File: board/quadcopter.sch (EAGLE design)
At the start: 41 parts, among them IC1 LD1117V33

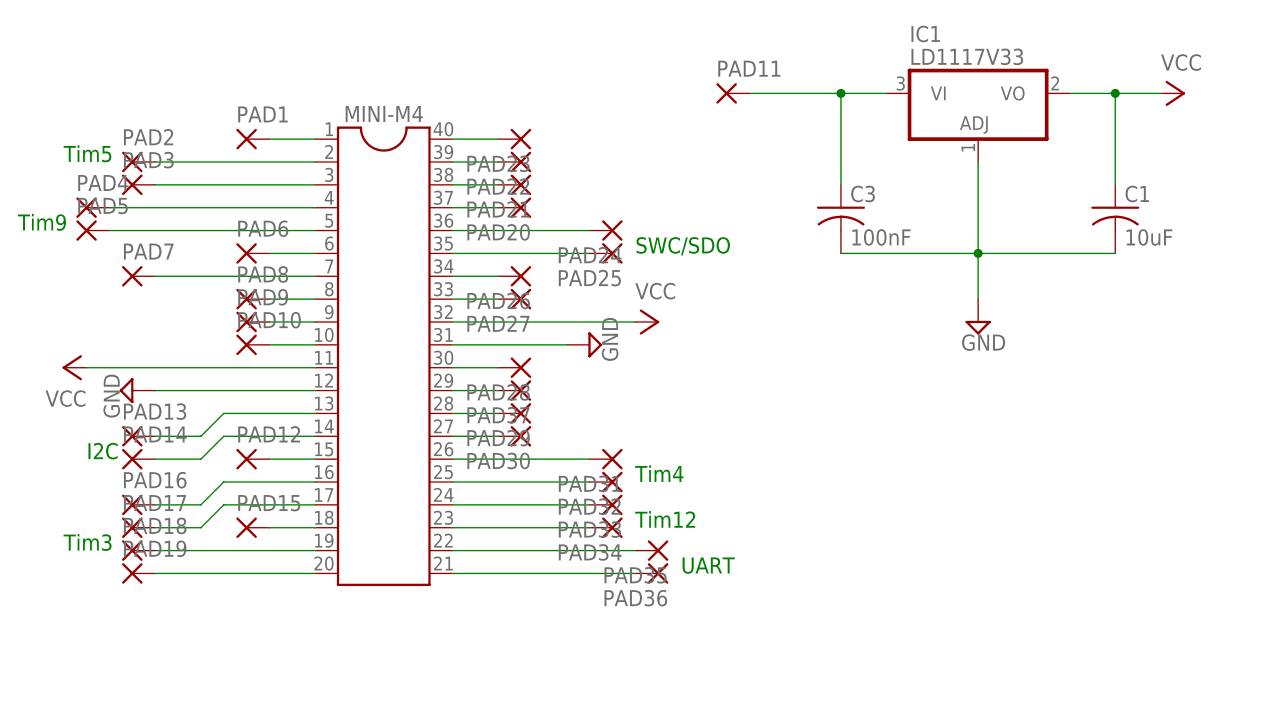
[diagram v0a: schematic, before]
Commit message: updated the board layout and routed the voltage regulator
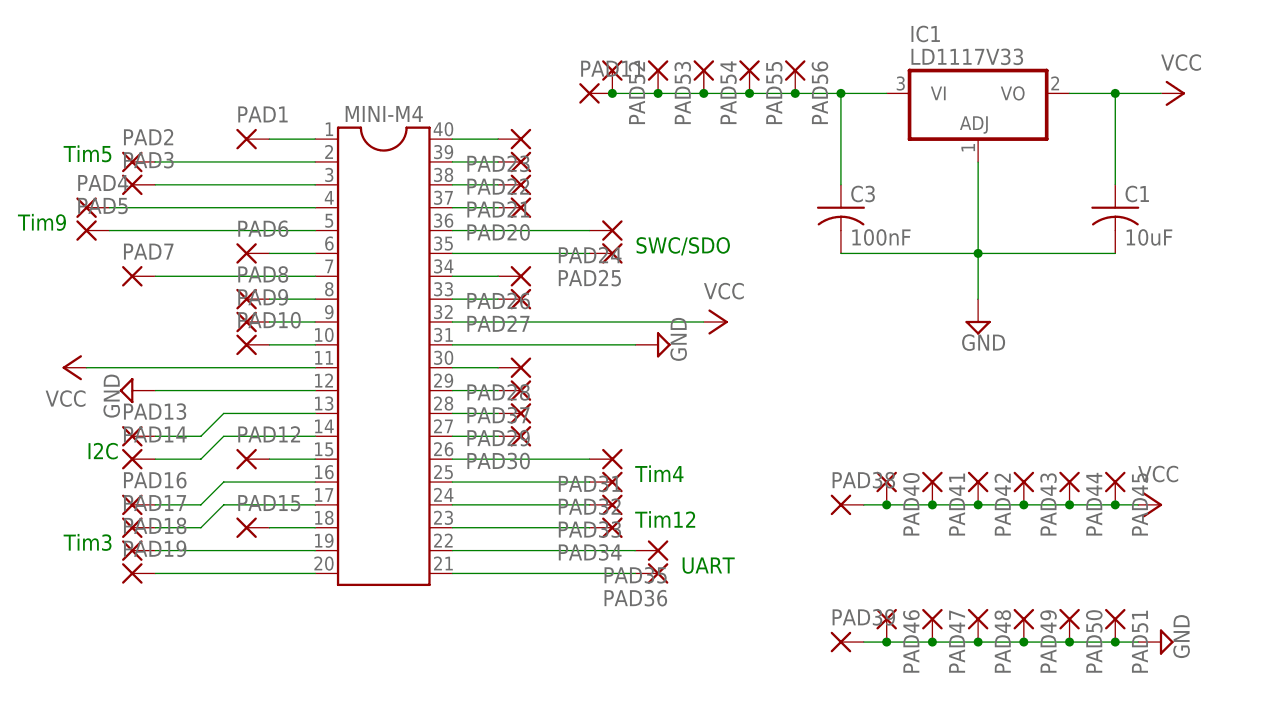
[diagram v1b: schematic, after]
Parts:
- added PAD38, PAD39, PAD40, PAD41, PAD42, PAD43, PAD44, PAD45, PAD46, PAD47, PAD48, PAD49, PAD50, PAD51, PAD52, PAD53, PAD54, PAD55, PAD56: (no value), wirepad:1,6/0,8
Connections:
- net GND: now also PAD39.P, PAD46.P, PAD47.P, PAD48.P, PAD49.P, PAD50.P, PAD51.P
- net N$15: now also PAD52.P, PAD53.P, PAD54.P, PAD55.P, PAD56.P
- net VCC: now also PAD38.P, PAD40.P, PAD41.P, PAD42.P, PAD43.P, PAD44.P, PAD45.P
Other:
- moved on the sheet: PAD11
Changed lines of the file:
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@@
 <part name="PAD22" library="wirepad" deviceset="1,6/0,8" device=""/>
 <part name="PAD23" library="wirepad" deviceset="1,6/0,8" device=""/>
-<part name="PAD11" library="wirepad" deviceset="1,6/0,8" device=""/>
 <part name="PAD7" library="wirepad" deviceset="1,6/0,8" device=""/>
 <part name="PAD37" library="wirepad" deviceset="1,6/0,8" device=""/>
+<part name="PAD11" library="wirepad" deviceset="1,6/0,8" device=""/>
+<part name="P+4" library="supply1" deviceset="VCC" device=""/>
+<part name="SUPPLY4" library="supply2" deviceset="GND" device=""/>
+<part name="PAD38" library="wirepad" deviceset="1,6/0,8" device=""/>
+<part name="PAD39" library="wirepad" deviceset="1,6/0,8" device=""/>
+<part name="PAD40" library="wirepad" deviceset="1,6/0,8" device=""/>
+<part name="PAD41" library="wirepad" deviceset="1,6/0,8" device=""/>
+<part name="PAD42" library="wirepad" deviceset="1,6/0,8" device=""/>
+<part name="PAD43" library="wirepad" deviceset="1,6/0,8" device=""/>
+<part name="PAD44" library="wirepad" deviceset="1,6/0,8" device=""/>
+<part name="PAD45" library="wirepad" deviceset="1,6/0,8" device=""/>
+<part name="PAD46" library="wirepad" deviceset="1,6/0,8" device=""/>
+<part name="PAD47" library="wirepad" deviceset="1,6/0,8" device=""/>
+<part name="PAD48" library="wirepad" deviceset="1,6/0,8" device=""/>
+<part name="PAD49" library="wirepad" deviceset="1,6/0,8" device=""/>
+<part name="PAD50" library="wirepad" deviceset="1,6/0,8" device=""/>
+<part name="PAD51" library="wirepad" deviceset="1,6/0,8" device=""/>
+<part name="PAD52" library="wirepad" deviceset="1,6/0,8" device=""/>
+<part name="PAD53" library="wirepad" deviceset="1,6/0,8" device=""/>
+<part name="PAD54" library="wirepad" deviceset="1,6/0,8" device=""/>
+<part name="PAD55" library="wirepad" deviceset="1,6/0,8" device=""/>
+<part name="PAD56" library="wirepad" deviceset="1,6/0,8" device=""/>
 </parts>
 <sheets>
@@
 <instance part="MINI-M4" gate="G$1" x="66.04" y="43.18"/>
 <instance part="SUPPLY1" gate="GND" x="38.1" y="38.1" rot="R270"/>
-<instance part="SUPPLY2" gate="GND" x="88.9" y="43.18" rot="R90"/>
+<instance part="SUPPLY2" gate="GND" x="96.52" y="43.18" rot="R90"/>
 <instance part="P+1" gate="VCC" x="30.48" y="40.64" rot="R90"/>
-<instance part="P+2" gate="VCC" x="96.52" y="45.72" rot="R270"/>
+<instance part="P+2" gate="VCC" x="104.14" y="45.72" rot="R270"/>
 <instance part="IC1" gate="A1" x="132.08" y="68.58"/>
 <instance part="C1" gate="G$1" x="147.32" y="58.42"/>
@@
 <instance part="PAD22" gate="P" x="81.28" y="63.5" rot="R180"/>
 <instance part="PAD23" gate="P" x="81.28" y="66.04" rot="R180"/>
-<instance part="PAD11" gate="P" x="104.14" y="71.12"/>
 <instance part="PAD7" gate="P" x="38.1" y="50.8"/>
 <instance part="PAD37" gate="P" x="81.28" y="38.1" rot="R180"/>
+<instance part="PAD11" gate="P" x="88.9" y="71.12"/>
+<instance part="P+4" gate="VCC" x="152.4" y="25.4" rot="R270"/>
+<instance part="SUPPLY4" gate="GND" x="152.4" y="10.16" rot="R90"/>
+<instance part="PAD38" gate="P" x="116.84" y="25.4"/>
+<instance part="PAD39" gate="P" x="116.84" y="10.16"/>
+<instance part="PAD40" gate="P" x="121.92" y="27.94" rot="R270"/>
+<instance part="PAD41" gate="P" x="127" y="27.94" rot="R270"/>
+<instance part="PAD42" gate="P" x="132.08" y="27.94" rot="R270"/>
+<instance part="PAD43" gate="P" x="137.16" y="27.94" rot="R270"/>
+<instance part="PAD44" gate="P" x="142.24" y="27.94" rot="R270"/>
+<instance part="PAD45" gate="P" x="147.32" y="27.94" rot="R270"/>
+<instance part="PAD46" gate="P" x="121.92" y="12.7" rot="R270"/>
+<instance part="PAD47" gate="P" x="127" y="12.7" rot="R270"/>
+<instance part="PAD48" gate="P" x="132.08" y="12.7" rot="R270"/>
+<instance part="PAD49" gate="P" x="137.16" y="12.7" rot="R270"/>
+<instance part="PAD50" gate="P" x="142.24" y="12.7" rot="R270"/>
+<instance part="PAD51" gate="P" x="147.32" y="12.7" rot="R270"/>
+<instance part="PAD52" gate="P" x="91.44" y="73.66" rot="R270"/>
+<instance part="PAD53" gate="P" x="96.52" y="73.66" rot="R270"/>
+<instance part="PAD54" gate="P" x="101.6" y="73.66" rot="R270"/>
+<instance part="PAD55" gate="P" x="106.68" y="73.66" rot="R270"/>
+<instance part="PAD56" gate="P" x="111.76" y="73.66" rot="R270"/>
 </instances>
 <busses>
@@
 <pinref part="MINI-M4" gate="G$1" pin="31"/>
 <pinref part="SUPPLY2" gate="GND" pin="GND"/>
-<wire x1="73.66" y1="43.18" x2="86.36" y2="43.18" width="0.1524" layer="91"/>
+<wire x1="73.66" y1="43.18" x2="93.98" y2="43.18" width="0.1524" layer="91"/>
 </segment>
 <segment>
@@
 <wire x1="132.08" y1="53.34" x2="147.32" y2="53.34" width="0.1524" layer="91"/>
 </segment>
+<segment>
+<pinref part="PAD39" gate="P" pin="P"/>
+<pinref part="SUPPLY4" gate="GND" pin="GND"/>
+<wire x1="119.38" y1="10.16" x2="121.92" y2="10.16" width="0.1524" layer="91"/>
+<pinref part="PAD46" gate="P" pin="P"/>
+<wire x1="121.92" y1="10.16" x2="127" y2="10.16" width="0.1524" layer="91"/>
+<junction x="121.92" y="10.16"/>
+<pinref part="PAD47" gate="P" pin="P"/>
+<wire x1="127" y1="10.16" x2="132.08" y2="10.16" width="0.1524" layer="91"/>
+<junction x="127" y="10.16"/>
+<pinref part="PAD48" gate="P" pin="P"/>
+<wire x1="132.08" y1="10.16" x2="137.16" y2="10.16" width="0.1524" layer="91"/>
+<junction x="132.08" y="10.16"/>
+<pinref part="PAD49" gate="P" pin="P"/>
+<wire x1="137.16" y1="10.16" x2="142.24" y2="10.16" width="0.1524" layer="91"/>
+<junction x="137.16" y="10.16"/>
+<pinref part="PAD50" gate="P" pin="P"/>
+<wire x1="142.24" y1="10.16" x2="147.32" y2="10.16" width="0.1524" layer="91"/>
+<junction x="142.24" y="10.16"/>
+<pinref part="PAD51" gate="P" pin="P"/>
+<wire x1="147.32" y1="10.16" x2="149.86" y2="10.16" width="0.1524" layer="91"/>
+<junction x="147.32" y="10.16"/>
+</segment>
 </net>
 <net name="VCC" class="0">
@@
 <pinref part="MINI-M4" gate="G$1" pin="32"/>
 <pinref part="P+2" gate="VCC" pin="VCC"/>
-<wire x1="73.66" y1="45.72" x2="93.98" y2="45.72" width="0.1524" layer="91"/>
+<wire x1="73.66" y1="45.72" x2="101.6" y2="45.72" width="0.1524" layer="91"/>
 </segment>
 <segment>
@@
 <junction x="147.32" y="71.12"/>
 </segment>
+<segment>
+<pinref part="PAD38" gate="P" pin="P"/>
+<pinref part="P+4" gate="VCC" pin="VCC"/>
+<wire x1="119.38" y1="25.4" x2="121.92" y2="25.4" width="0.1524" layer="91"/>
+<pinref part="PAD40" gate="P" pin="P"/>
+<wire x1="121.92" y1="25.4" x2="127" y2="25.4" width="0.1524" layer="91"/>
+<junction x="121.92" y="25.4"/>
+<pinref part="PAD41" gate="P" pin="P"/>
+<wire x1="127" y1="25.4" x2="132.08" y2="25.4" width="0.1524" layer="91"/>
+<junction x="127" y="25.4"/>
+<pinref part="PAD42" gate="P" pin="P"/>
+<wire x1="132.08" y1="25.4" x2="137.16" y2="25.4" width="0.1524" layer="91"/>
+<junction x="132.08" y="25.4"/>
+<pinref part="PAD43" gate="P" pin="P"/>
+<wire x1="137.16" y1="25.4" x2="142.24" y2="25.4" width="0.1524" layer="91"/>
+<junction x="137.16" y="25.4"/>
+<pinref part="PAD44" gate="P" pin="P"/>
+<wire x1="142.24" y1="25.4" x2="147.32" y2="25.4" width="0.1524" layer="91"/>
+<junction x="142.24" y="25.4"/>
+<pinref part="PAD45" gate="P" pin="P"/>
+<wire x1="147.32" y1="25.4" x2="149.86" y2="25.4" width="0.1524" layer="91"/>
+<junction x="147.32" y="25.4"/>
+</segment>
 </net>
 <net name="N$11" class="0">
@@
 <wire x1="116.84" y1="71.12" x2="116.84" y2="60.96" width="0.1524" layer="91"/>
 <pinref part="PAD11" gate="P" pin="P"/>
-<wire x1="106.68" y1="71.12" x2="116.84" y2="71.12" width="0.1524" layer="91"/>
+<wire x1="91.44" y1="71.12" x2="96.52" y2="71.12" width="0.1524" layer="91"/>
 <junction x="116.84" y="71.12"/>
-</segment>
-</net>
+<pinref part="PAD52" gate="P" pin="P"/>
+<junction x="91.44" y="71.12"/>
+<pinref part="PAD53" gate="P" pin="P"/>
+<wire x1="96.52" y1="71.12" x2="101.6" y2="71.12" width="0.1524" layer="91"/>
+<junction x="96.52" y="71.12"/>
+<pinref part="PAD54" gate="P" pin="P"/>
+<wire x1="101.6" y1="71.12" x2="106.68" y2="71.12" width="0.1524" layer="91"/>
+<junction x="101.6" y="71.12"/>
+<pinref part="PAD55" gate="P" pin="P"/>
+<wire x1="106.68" y1="71.12" x2="111.76" y2="71.12" width="0.1524" layer="91"/>
+<junction x="106.68" y="71.12"/>
+<pinref part="PAD56" gate="P" pin="P"/>
+<wire x1="111.76" y1="71.12" x2="116.84" y2="71.12" width="0.1524" layer="91"/>
+<junction x="111.76" y="71.12"/>
+</segment>
+</net>

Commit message: updated quadcopter board to accomodate the 9dof
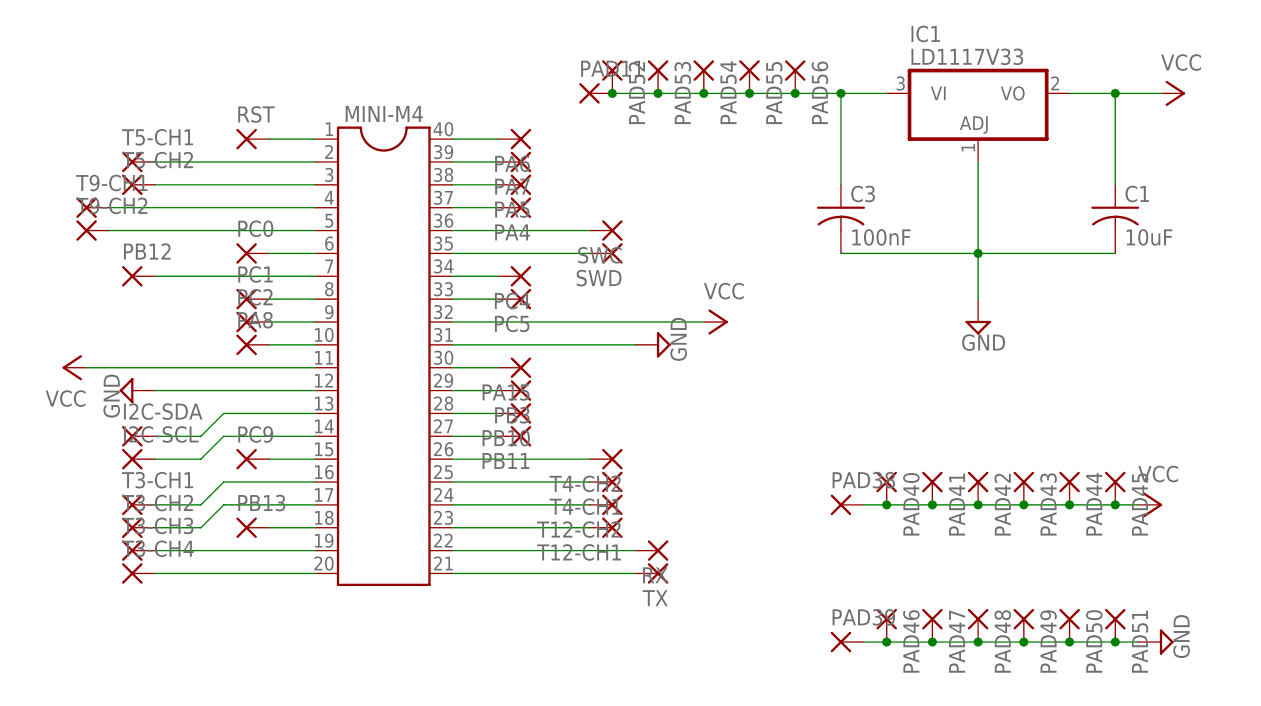
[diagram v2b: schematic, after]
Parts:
- renumbered PAD1 to RST, PAD10 to PA8, PAD12 to PC9, PAD13 to I2C-SDA, PAD14 to I2C-SCL, PAD15 to PB13, PAD16 to T3-CH1, PAD17 to T3-CH2, PAD18 to T3-CH3, PAD19 to T3-CH4, PAD2 to T5-CH1, PAD20 to PA4, PAD21 to PA5, PAD22 to PA7, PAD23 to PA6, PAD24 to SWC, PAD25 to SWD, PAD26 to PC4, PAD27 to PC5, PAD28 to PA15, PAD29 to PB10, PAD3 to T5-CH2, PAD30 to PB11, PAD31 to T4-CH2, PAD32 to T4-CH1, PAD33 to T12-CH2, PAD34 to T12-CH1, PAD35 to RX, PAD36 to TX, PAD37 to PB3, PAD4 to T9-CH1, PAD5 to T9-CH2, PAD6 to PC0, PAD7 to PB12, PAD8 to PC1, PAD9 to PC2
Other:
- note removed: "I2C"
- note removed: "SWC/SDO"
- note removed: "Tim12"
- note removed: "Tim3"
- note removed: "Tim4"
- note removed: "Tim5"
- note removed: "Tim9"
- note removed: "UART"

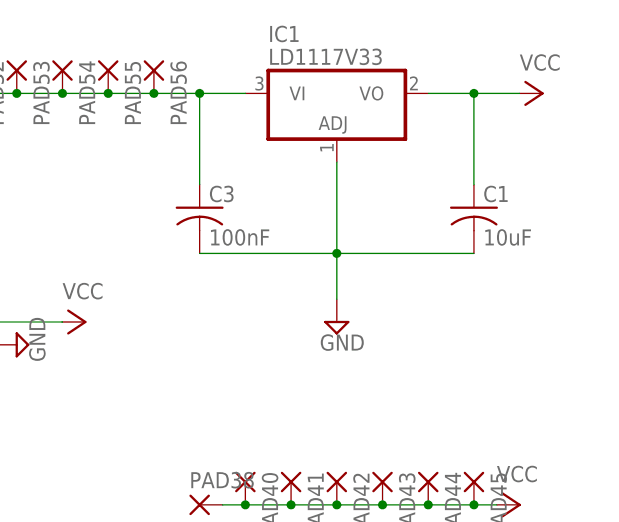
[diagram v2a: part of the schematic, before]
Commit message: added the capacitor label to the board because I keep forgetting what it is
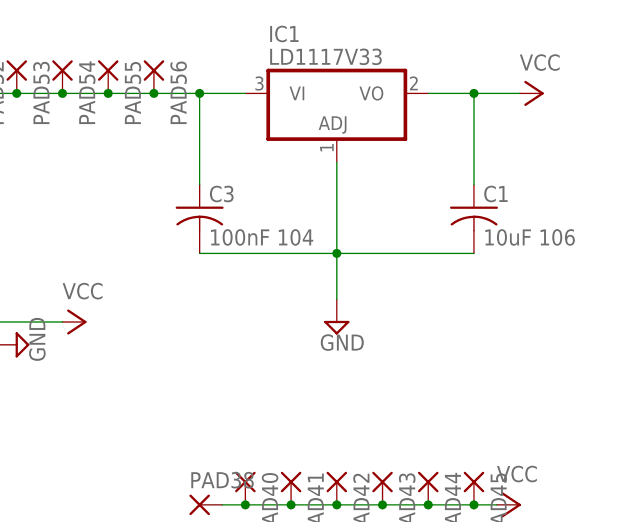
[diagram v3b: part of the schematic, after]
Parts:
- C1: value 10uF -> 10uF 106
- C3: value 100nF -> 100nF 104
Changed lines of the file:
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@@
 <part name="P+2" library="supply1" deviceset="VCC" device=""/>
 <part name="IC1" library="linear" deviceset="*317" device="T" value="LD1117V33"/>
-<part name="C1" library="rcl" deviceset="C-US" device="025-040X050" value="10uF"/>
-<part name="C3" library="rcl" deviceset="C-US" device="025-040X050" value="100nF"/>
+<part name="C1" library="rcl" deviceset="C-US" device="025-040X050" value="10uF 106"/>
+<part name="C3" library="rcl" deviceset="C-US" device="025-040X050" value="100nF 104"/>
 <part name="SUPPLY3" library="supply2" deviceset="GND" device=""/>
 <part name="P+3" library="supply1" deviceset="VCC" device=""/>
